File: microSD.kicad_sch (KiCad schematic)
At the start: 8 parts, among them IC3 74HC4050D, IC4 LP2985A, J5 microSD

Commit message: added Arduino UNO R4 in root sheet
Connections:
- net D4 renamed CS
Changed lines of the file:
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@@
 		)
 	)
-	(hierarchical_label "D4"
+	(hierarchical_label "CS"
 		(shape input)
 		(at 177.8 127 180)

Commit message: added pyrano, anemo, AM2315C, power supply, LEDs, switch and FPC connector in schematic
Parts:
- C21: renamed from C11; Component package type 0805 -> C_0805
- renumbered C10 to C20, D6 to D14, J5 to J13, J6 to J14, R14 to R25
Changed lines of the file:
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@@
 		(on_board yes)
 		(dnp no)
-		(property "Reference" "#PWR04"
+		(property "Reference" "#PWR021"
 			(at 120.65 85.09 0)
 			(effects
@@
 			(project "testing-station"
 				(path "/ed3950ec-e24f-4dd6-b9cc-eca012f1333b/535b300a-c6bc-4326-93aa-a53347054cf5"
-					(reference "#PWR04")
+					(reference "#PWR021")
 					(unit 1)
 				)
@@
 					(size 1.27 1.27)
 				)
+				(hide yes)
 			)
 		)
@@
 		(on_board yes)
 		(dnp no)
-		(property "Reference" "D6"
+		(property "Reference" "D14"
 			(at 136.906 75.946 0)
 			(effects
@@
 			(project "testing-station"
 				(path "/ed3950ec-e24f-4dd6-b9cc-eca012f1333b/535b300a-c6bc-4326-93aa-a53347054cf5"
-					(reference "D6")
+					(reference "D14")
 					(unit 1)
 				)
@@
 		(on_board yes)
 		(dnp no)
-		(property "Reference" "R14"
+		(property "Reference" "R25"
 			(at 145.796 72.644 90)
 			(effects
@@
 			(project "testing-station"
 				(path "/ed3950ec-e24f-4dd6-b9cc-eca012f1333b/535b300a-c6bc-4326-93aa-a53347054cf5"
-					(reference "R14")
+					(reference "R25")
 					(unit 1)
 				)
@@
 		(on_board yes)
 		(dnp no)
-		(property "Reference" "#PWR03"
+		(property "Reference" "#PWR020"
 			(at 154.94 78.74 0)
 			(effects
@@
 			(project "testing-station"
 				(path "/ed3950ec-e24f-4dd6-b9cc-eca012f1333b/535b300a-c6bc-4326-93aa-a53347054cf5"
-					(reference "#PWR03")
+					(reference "#PWR020")
 					(unit 1)
 				)
@@
 		(on_board yes)
 		(dnp no)
-		(property "Reference" "C11"
-			(at 112.268 113.792 0)
+		(property "Reference" "C21"
+			(at 112.776 112.014 0)
 			(effects
 				(font
@@
 		)
 		(property "Value" "0.1uF"
-			(at 118.872 113.792 0)
+			(at 111.252 115.57 0)
 			(effects
 				(font
@@
 			)
 		)
-		(property "Component package type" "0805"
+		(property "Component package type" "C_0805"
 			(at 116.84 113.03 0)
 			(effects
@@
 			(project "testing-station"
 				(path "/ed3950ec-e24f-4dd6-b9cc-eca012f1333b/535b300a-c6bc-4326-93aa-a53347054cf5"
-					(reference "C11")
+					(reference "C21")
 					(unit 1)
 				)
@@
 		(on_board yes)
 		(dnp no)
-		(property "Reference" "J5"
+		(property "Reference" "J13"
 			(at 181.61 63.246 0)
 			(effects
@@
 			(project "testing-station"
 				(path "/ed3950ec-e24f-4dd6-b9cc-eca012f1333b/535b300a-c6bc-4326-93aa-a53347054cf5"
-					(reference "J5")
+					(reference "J13")
 					(unit 1)
 				)
@@
 		(on_board yes)
 		(dnp no)
-		(property "Reference" "#PWR01"
+		(property "Reference" "#PWR018"
 			(at 91.44 74.93 0)
 			(effects
@@
 			(project "testing-station"
 				(path "/ed3950ec-e24f-4dd6-b9cc-eca012f1333b/535b300a-c6bc-4326-93aa-a53347054cf5"
-					(reference "#PWR01")
+					(reference "#PWR018")
 					(unit 1)
 				)
@@
 		(on_board yes)
 		(dnp no)
-		(property "Reference" "C10"
-			(at 93.218 113.792 0)
+		(property "Reference" "C20"
+			(at 93.726 112.014 0)
 			(effects
 				(font
@@
 		)
 		(property "Value" "10uF"
-			(at 99.822 113.792 0)
+			(at 92.71 115.57 0)
 			(effects
 				(font
@@
 			(project "testing-station"
 				(path "/ed3950ec-e24f-4dd6-b9cc-eca012f1333b/535b300a-c6bc-4326-93aa-a53347054cf5"
-					(reference "C10")
+					(reference "C20")
 					(unit 1)
 				)
@@
 		(on_board yes)
 		(dnp no)
-		(property "Reference" "#PWR02"
+		(property "Reference" "#PWR019"
 			(at 120.65 77.47 0)
 			(effects
@@
 			(project "testing-station"
 				(path "/ed3950ec-e24f-4dd6-b9cc-eca012f1333b/535b300a-c6bc-4326-93aa-a53347054cf5"
-					(reference "#PWR02")
+					(reference "#PWR019")
 					(unit 1)
 				)
@@
 		(on_board yes)
 		(dnp no)
-		(property "Reference" "J6"
+		(property "Reference" "J14"
 			(at 191.77 108.458 0)
 			(effects
@@
 			(project "testing-station"
 				(path "/ed3950ec-e24f-4dd6-b9cc-eca012f1333b/535b300a-c6bc-4326-93aa-a53347054cf5"
-					(reference "J6")
+					(reference "J14")
 					(unit 1)
 				)
@@
 		(on_board yes)
 		(dnp no)
-		(property "Reference" "#PWR05"
+		(property "Reference" "#PWR022"
 			(at 91.44 97.79 0)
 			(effects
@@
 			(project "testing-station"
 				(path "/ed3950ec-e24f-4dd6-b9cc-eca012f1333b/535b300a-c6bc-4326-93aa-a53347054cf5"
-					(reference "#PWR05")
+					(reference "#PWR022")
 					(unit 1)
 				)
@@
 					(size 1.27 1.27)
 				)
+				(hide yes)
 			)
 		)
@@
 		(on_board yes)
 		(dnp no)
-		(property "Reference" "#PWR06"
+		(property "Reference" "#PWR023"
 			(at 203.2 101.6 0)
 			(effects
@@
 			(project "testing-station"
 				(path "/ed3950ec-e24f-4dd6-b9cc-eca012f1333b/535b300a-c6bc-4326-93aa-a53347054cf5"
-					(reference "#PWR06")
-					(unit 1)
-				)
+					(reference "#PWR023")
+					(unit 1)
+				)

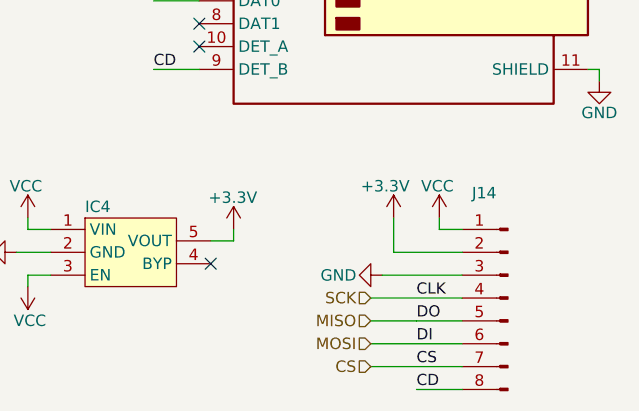
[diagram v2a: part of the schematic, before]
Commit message: removed connectors from modules
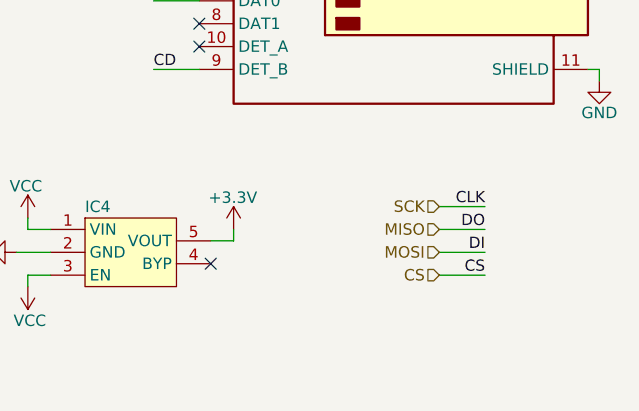
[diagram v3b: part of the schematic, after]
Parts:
- removed J14: ~, Connector_PinHeader_2.54mm:PinHeader_1x08_P2.54mm_Vertical, symbol Connector:Conn_01x08_Pin

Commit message: added microSD external files
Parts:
- IC3: symbol external_library:74HC4050D -> external_symbols:74HC4050D
- IC4: symbol external_library:LP2985A -> external_symbols:LP2985A
- J13: footprint external_footprints:GCT_MEM2061-01-188-00-A_REVA -> external_footprints:MEM2061-01-188-00-A
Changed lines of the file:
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@@
 	)
 	(symbol
-		(lib_id "external_library:74HC4050D")
+		(lib_id "external_symbols:74HC4050D")
 		(at 96.52 91.44 0)
 		(unit 1)
@@
 			)
 		)
-		(property "Footprint" "external_footprints:GCT_MEM2061-01-188-00-A_REVA"
+		(property "Footprint" "external_footprints:MEM2061-01-188-00-A"
 			(at 233.68 63.5 0)
 			(effects
@@
 	)
 	(symbol
-		(lib_id "external_library:LP2985A")
+		(lib_id "external_symbols:LP2985A")
 		(at 146.05 118.11 0)
 		(unit 1)

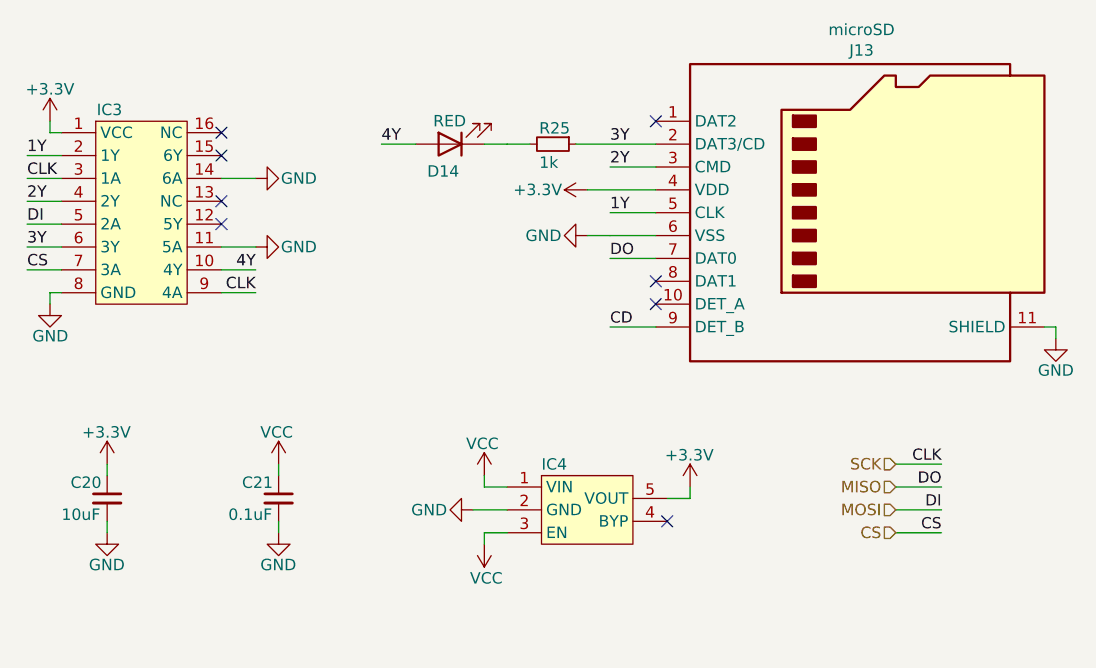
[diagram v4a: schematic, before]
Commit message: removed voltage regulators of each individual module
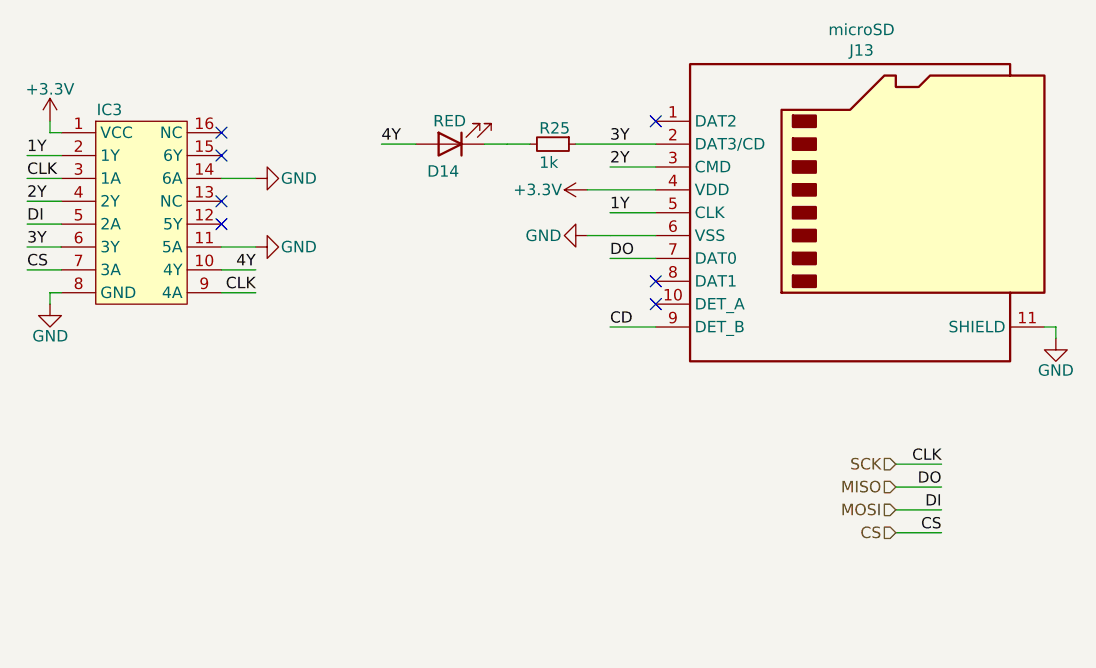
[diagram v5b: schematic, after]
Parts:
- removed C20: 10uF, Capacitor_SMD:C_0805_2012Metric, symbol Device:C_Small
- removed C21: 0.1uF, Capacitor_SMD:C_0805_2012Metric, symbol Device:C_Small
- removed IC4: LP2985A, Package_TO_SOT_SMD:SOT-23-5, symbol external_symbols:LP2985A
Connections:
- no-connect marks 8 -> 7

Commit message: BOM update
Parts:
- D14: Component package type 0805 -> (none)
- IC3: Component package type 16-SOIC -> (none)
- J13: Component package type / -> (none)
- R25: Component package type R_0805 -> (none)
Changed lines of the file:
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@@
-			)
-		)
-		(property "Component package type" "16-SOIC"
-			(at 96.52 91.44 0)
-			(effects
-				(font
-					(size 1.27 1.27)
-				)
-				(hide yes)
 			)
 		)
@@
 			)
 		)
-		(property "Component package type" "0805"
-			(at 135.89 73.66 0)
-			(effects
-				(font
-					(size 1.27 1.27)
-				)
-				(hide yes)
-			)
-		)
 		(pin "1"
 		)
@@
 			)
 		)
-		(property "Component package type" "R_0805"
-			(at 147.32 73.66 90)
-			(effects
-				(font
-					(size 1.27 1.27)
-				)
-				(hide yes)
-			)
-		)
 		(pin "1"
 		)
@@
 			(at 181.61 81.28 0)
 			(effects
-				(font
-					(size 1.27 1.27)
-				)
-				(hide yes)
-			)
-		)
-		(property "Component package type" "/"
-			(at 181.61 81.28 0)
-			(effects
